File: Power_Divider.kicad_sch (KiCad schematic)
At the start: 46 parts, among them J16 Conn_01x02_Pin, J18 2118714-2, J9 2118714-2, P10 CONUFL001-SMD-T, P11 CONUFL001-SMD-T, P12 CONUFL001-SMD-T, P8 CONUFL001-SMD-T, P9 CONUFL001-SMD-T, U25 QPL9547, U7 MAX4995AAUT+T

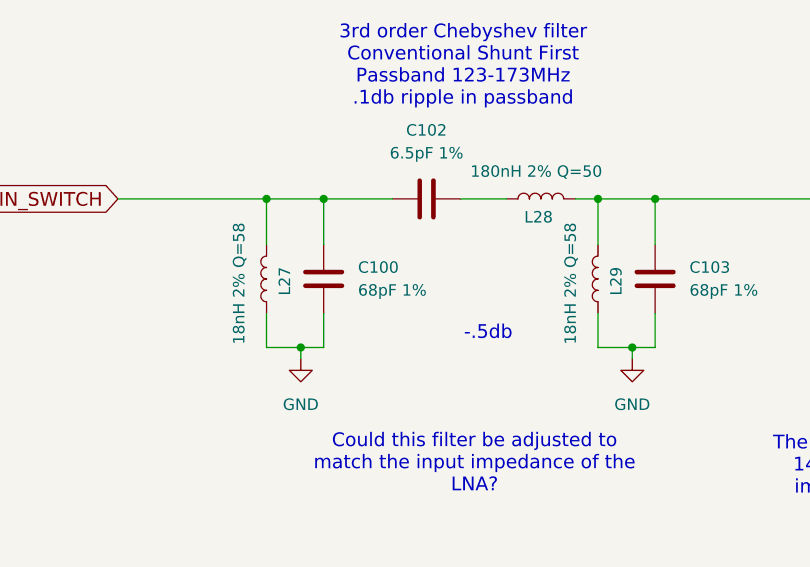
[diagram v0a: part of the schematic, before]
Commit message: Change the inductors on the RF input filter
Use lower resistance ones with higher Q.

Signed-off-by: Corey Minyard <corey@minyard.net>
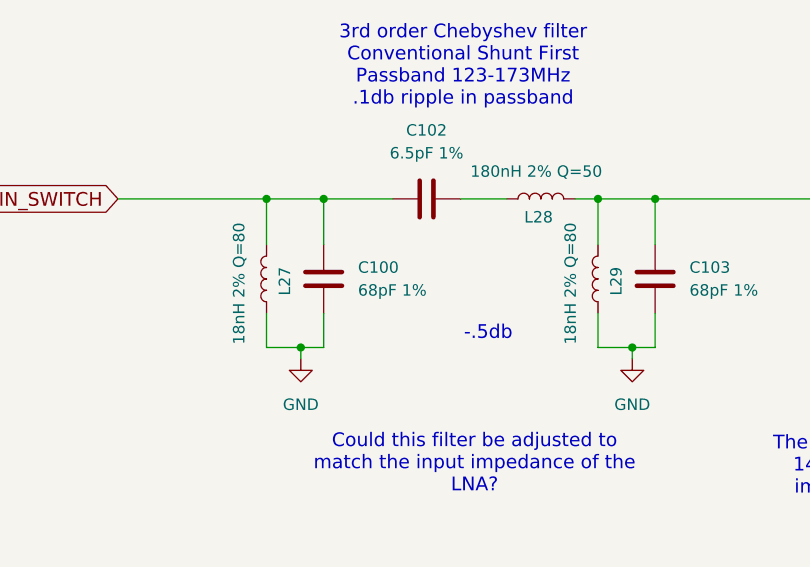
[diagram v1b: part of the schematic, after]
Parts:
- L27, L29: value 18nH 2% Q=58 -> 18nH 2% Q=80; footprint Inductor_SMD:L_0402_1005Metric_Pad0.77x0.64mm_HandSolder -> Inductor_SMD:L_0603_1608Metric_Pad1.05x0.95mm_HandSolder
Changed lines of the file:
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@@
 			)
 		)
-		(property "Value" "18nH 2% Q=58"
+		(property "Value" "18nH 2% Q=80"
 			(at 59.182 152.908 90)
 			(effects
@@
 			)
 		)
-		(property "Footprint" "Inductor_SMD:L_0402_1005Metric_Pad0.77x0.64mm_HandSolder"
+		(property "Footprint" "Inductor_SMD:L_0603_1608Metric_Pad1.05x0.95mm_HandSolder"
 			(at 62.23 152.4 0)
 			(effects
@@
 			)
 		)
-		(property "Value" "18nH 2% Q=58"
+		(property "Value" "18nH 2% Q=80"
 			(at 96.012 152.908 90)
 			(effects
@@
 			)
 		)
-		(property "Footprint" "Inductor_SMD:L_0402_1005Metric_Pad0.77x0.64mm_HandSolder"
+		(property "Footprint" "Inductor_SMD:L_0603_1608Metric_Pad1.05x0.95mm_HandSolder"
 			(at 99.06 152.4 0)
 			(effects

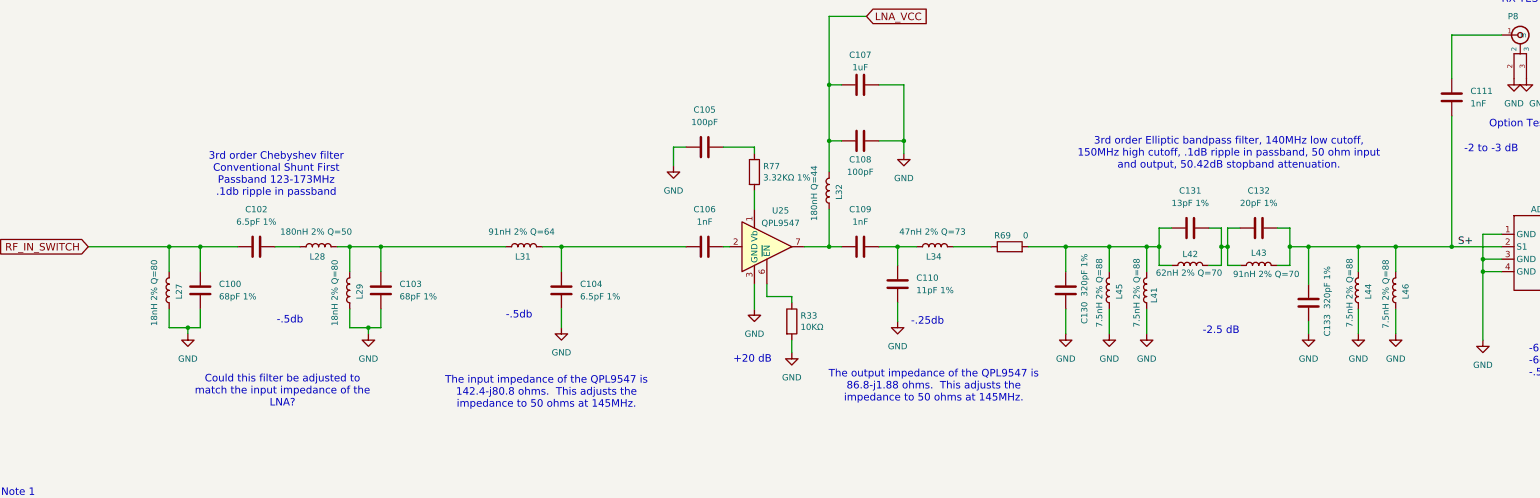
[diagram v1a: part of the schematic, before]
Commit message: Massive rework of filtering and inductors
Now that I know how inductors really work.

Signed-off-by: Corey Minyard <corey@minyard.net>
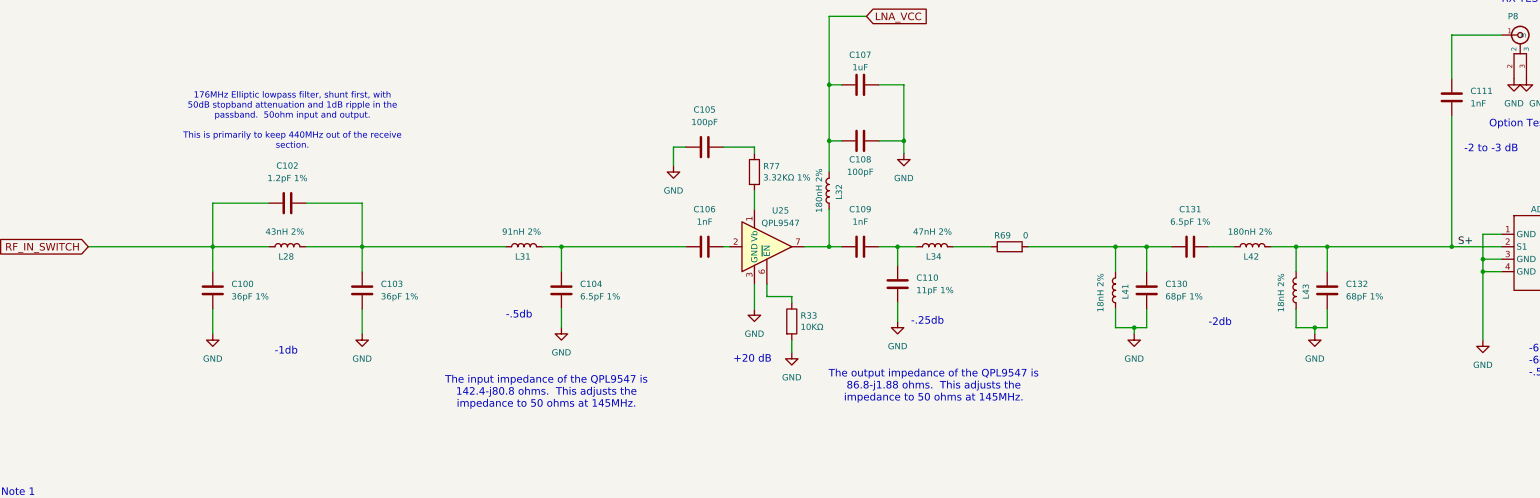
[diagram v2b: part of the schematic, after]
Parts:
- removed C133: 320pF 1%, Capacitor_SMD:C_0402_1005Metric_Pad0.74x0.62mm_HandSolder, symbol Device:C
- removed L27, L29: 18nH 2% Q=80, Inductor_SMD:L_0603_1608Metric_Pad1.05x0.95mm_HandSolder, symbol Device:L
- removed L44, L45, L46: 7.5nH 2% Q=88, Inductor_SMD:L_0603_1608Metric_Pad1.05x0.95mm_HandSolder, symbol Device:L
- C100, C103: value 68pF 1% -> 36pF 1%
- C102: value 6.5pF 1% -> 1.2pF 1%
- C130: value 320pF 1% -> 68pF 1%
- C131: value 13pF 1% -> 6.5pF 1%
- C132: value 20pF 1% -> 68pF 1%
- L28: value 180nH 2% Q=50 -> 43nH 2%
- L31: value 91nH 2% Q=64 -> 91nH 2%; footprint Inductor_SMD:L_0603_1608Metric_Pad1.05x0.95mm_HandSolder -> Inductor_SMD:L_0805_2012Metric_Pad1.05x1.20mm_HandSolder
- L32: value 180nH Q=44 -> 180nH 2%; footprint Inductor_SMD:L_0603_1608Metric_Pad1.05x0.95mm_HandSolder -> Inductor_SMD:L_0805_2012Metric_Pad1.05x1.20mm_HandSolder
- L34: value 47nH 2% Q=73 -> 47nH 2%
- L41: value 7.5nH 2% Q=88 -> 18nH 2%
- L42: value 62nH 2% Q=70 -> 180nH 2%; footprint Inductor_SMD:L_0805_2012Metric_Pad1.05x1.20mm_HandSolder -> Inductor_SMD:L_0805_2012Metric
- L43: value 91nH 2% Q=70 -> 18nH 2%; footprint Inductor_SMD:L_0805_2012Metric_Pad1.05x1.20mm_HandSolder -> Inductor_SMD:L_0603_1608Metric_Pad1.05x0.95mm_HandSolder
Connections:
- net GND: now also C132.1, L43.2
- net RF_IN_SWITCH: now also L28.2
- net S+: now also C132.2, L42.1; no longer C132.1
- net at C103.2, L28.1, L31.2: now also C102.1
- net at C130.2, C131.2, L41.1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: no longer L42.2
- new net: C131.1, L42.2
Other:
- note added: "-1db"
- note added: "-2db"
- note added: "176MHz Elliptic lowpass filter, shunt first, with 50dB stopband attenuation and 1dB ripple in the passband. 50ohm input and output. This is primarily to keep 440MHz out of the receive section."
- note removed: "-2.5 dB"
- note removed: "3rd order Chebyshev filter Conventional Shunt First Passband 123-173MHz .1db ripple in passband"
- note removed: "3rd order Elliptic bandpass filter, 140MHz low cutoff, 150MHz high cutoff, .1dB ripple in passband, 50 ohm input and output, 50.42dB stopband attenuation."
- note removed: "Could this filter be adjusted to match the input impedance of the LNA?"
- moved on the sheet: C100, C102, C103, L28

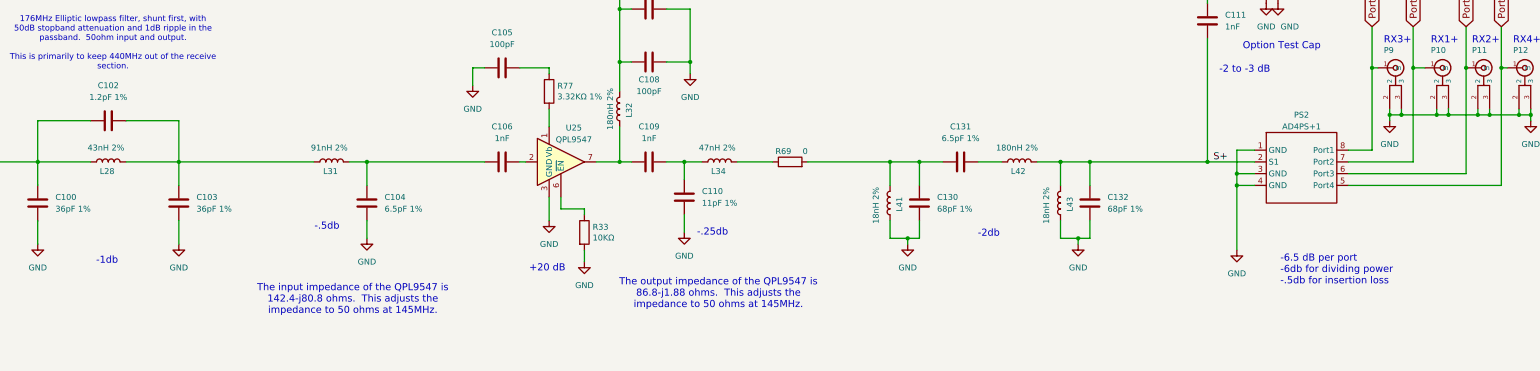
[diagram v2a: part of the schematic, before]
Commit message: Take into account capacitance of inductors
Signed-off-by: Corey Minyard <corey@minyard.net>
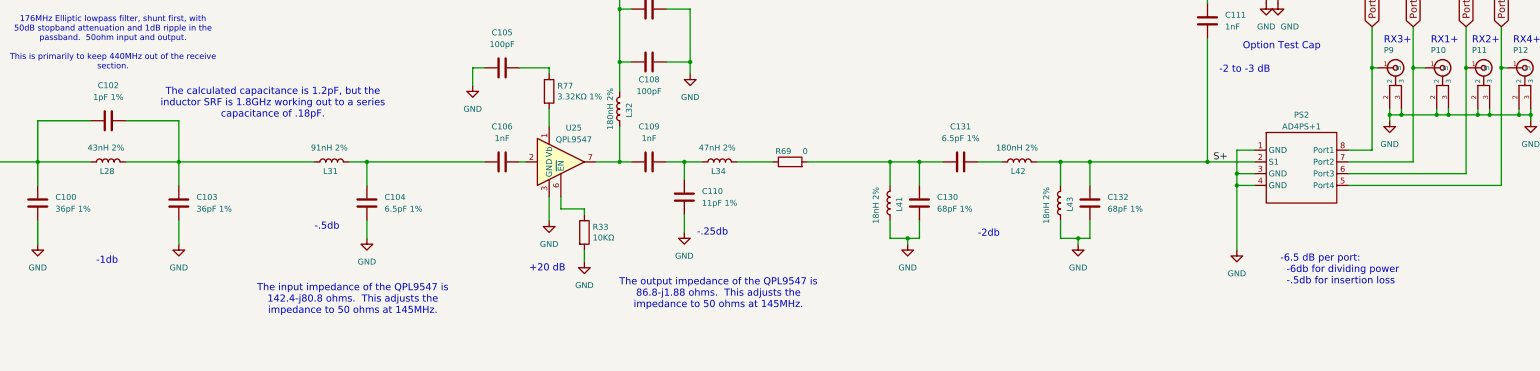
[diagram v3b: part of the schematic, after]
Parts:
- C102: value 1.2pF 1% -> 1pF 1%
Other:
- note added: "-6.5 dB per port: -6db for dividing power -.5db for insertion loss"
- note added: "The calculated capacitance is 1.2pF, but the inductor SRF is 1.8GHz working out to a series capacitance of .18pF."
- note removed: "-6.5 dB per port -6db for dividing power -.5db for insertion loss"
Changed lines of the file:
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@@
 		)
 	)
-	(text "-6.5 dB per port\n-6db for dividing power\n-.5db for insertion loss"
+	(text "-6.5 dB per port:\n  -6db for dividing power\n  -.5db for insertion loss"
 		(exclude_from_sim no)
 		(at 339.598 170.18 0)
@@
 		)
 	)
+	(text "The calculated capacitance is 1.2pF, but the\ninductor SRF is 1.8GHz working out to a series\ncapacitance of .18pF."
+		(exclude_from_sim no)
+		(at 121.92 130.81 0)
+		(effects
+			(font
+				(size 1.524 1.524)
+			)
+		)
+	)
 	(text "Note 3\nAll RF circuits must have at least 2 vias on \nall connections between PCB planes."
 		(exclude_from_sim no)
@@
 			)
 		)
-		(property "Value" "1.2pF 1%"
+		(property "Value" "1pF 1%"
 			(at 86.36 129.54 90)
 			(effects

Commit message: More simulation cleanups
Signed-off-by: Corey Minyard <corey@minyard.net>
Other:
- note added: "123-173MHz Chebychev bandpass filter, simulated from: * https://markimicrowave.com/technical-resources/tools/lc-filter-design-tool/ 3rd order, conventional shunt first, 123MHz low cutoff, 173MHz high cutoff, .10db ripple in passband, 50 ohm input, 50 ohm output impedance."
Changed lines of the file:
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@@
+		)
+	)
+	(text "123-173MHz Chebychev bandpass filter, simulated from:\n* https://markimicrowave.com/technical-resources/tools/lc-filter-design-tool/\n3rd order, conventional shunt first, 123MHz low cutoff, 173MHz high\ncutoff, .10db ripple in passband, 50 ohm input, 50 ohm output\nimpedance."
+		(exclude_from_sim no)
+		(at 273.812 127.254 0)
+		(effects
+			(font
+				(size 1.27 1.27)
+			)
 		)
 	)

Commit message: Minor fixes for BOM values
Signed-off-by: Corey Minyard <corey@minyard.net>
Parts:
- R69: value 0 -> 0Ω
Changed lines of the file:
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@@
 			)
 		)
-		(property "Value" "0"
+		(property "Value" "0Ω"
 			(at 237.49 141.224 90)
 			(effects

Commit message: A bunch of work on component selections
And little fixups for things I found.

Signed-off-by: Corey Minyard <corey@minyard.net>
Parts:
- C102: value 1pF 1% -> 1pF ±.05
- C104, C131: value 6.5pF 1% -> 6.5pF ±.1
- R33, R77: footprint Resistor_SMD:R_0603_1608Metric_Pad0.98x0.95mm_HandSolder -> Resistor_SMD:R_0402_1005Metric_Pad0.72x0.64mm_HandSolder
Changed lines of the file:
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@@
 			)
 		)
-		(property "Footprint" "Resistor_SMD:R_0603_1608Metric_Pad0.98x0.95mm_HandSolder"
+		(property "Footprint" "Resistor_SMD:R_0402_1005Metric_Pad0.72x0.64mm_HandSolder"
 			(at 179.832 128.27 90)
 			(effects
@@
 			)
 		)
-		(property "Footprint" "Resistor_SMD:R_0603_1608Metric_Pad0.98x0.95mm_HandSolder"
+		(property "Footprint" "Resistor_SMD:R_0402_1005Metric_Pad0.72x0.64mm_HandSolder"
 			(at 187.452 158.75 90)
 			(effects
@@
 			)
 		)
-		(property "Value" "6.5pF 1%"
+		(property "Value" "6.5pF ±.1"
 			(at 146.05 153.6699 0)
 			(effects
@@
 			)
 		)
-		(property "Value" "6.5pF 1%"
+		(property "Value" "6.5pF ±.1"
 			(at 270.51 138.43 90)
 			(effects
@@
 			)
 		)
-		(property "Value" "1pF 1%"
+		(property "Value" "1pF ±.05"
 			(at 86.36 129.54 90)
 			(effects

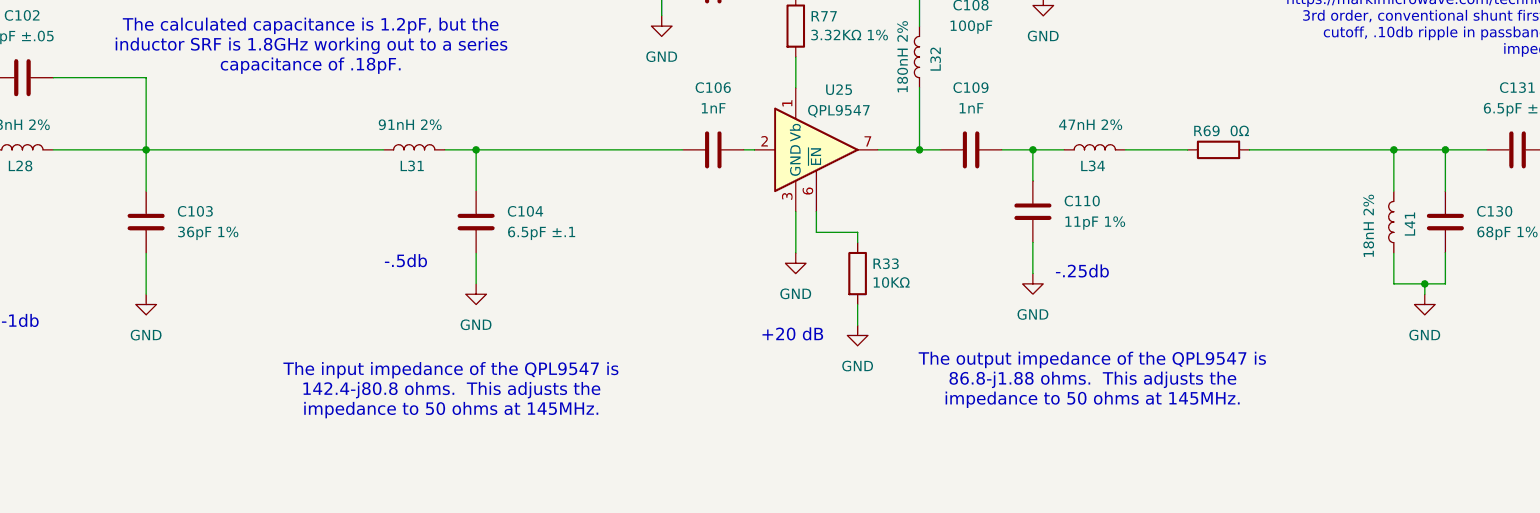
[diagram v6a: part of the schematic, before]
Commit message: Add some more UF.L connectors, clean up more stuff
Allow access to some more points in the RF chain.

Signed-off-by: Corey Minyard <corey@minyard.net>
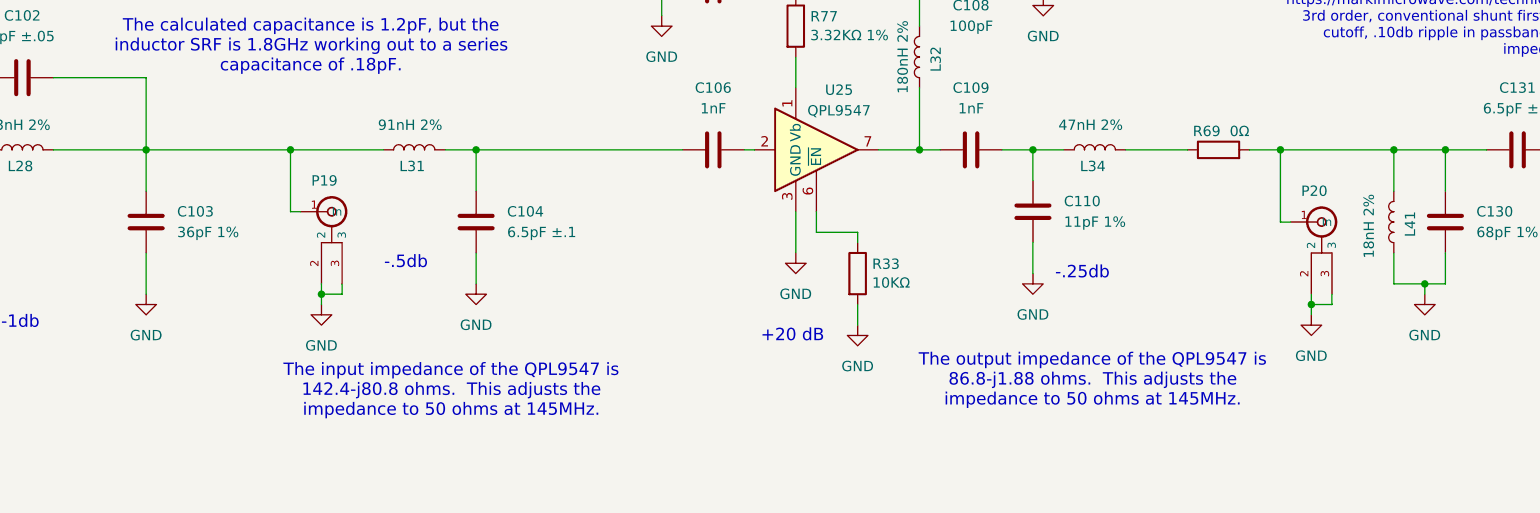
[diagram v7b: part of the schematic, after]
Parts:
- added P19, P20: CONUFL001-SMD-T, PacSatDev_misc:CONN1_CONUFL_TEC, symbol PACSAT_DEV_misc:U_FL
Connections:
- net GND: now also P19.2, P19.3, P20.2, P20.3
- net at C102.1, C103.2, L28.1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: now also P19.1 (In)
- net at C130.2, C131.2, L41.1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: now also P20.1 (In)

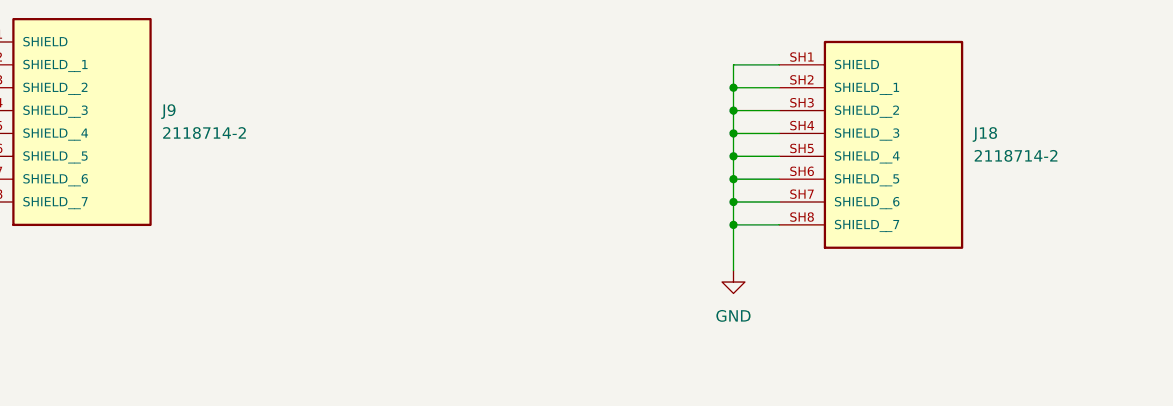
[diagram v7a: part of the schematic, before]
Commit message: Renumber shields and PC104 sockets
Separate out shields into their own designator category.

Make the PC104 sockets J1 and J2 to make it easier to move to other
boards.

Signed-off-by: Corey Minyard <corey@minyard.net>
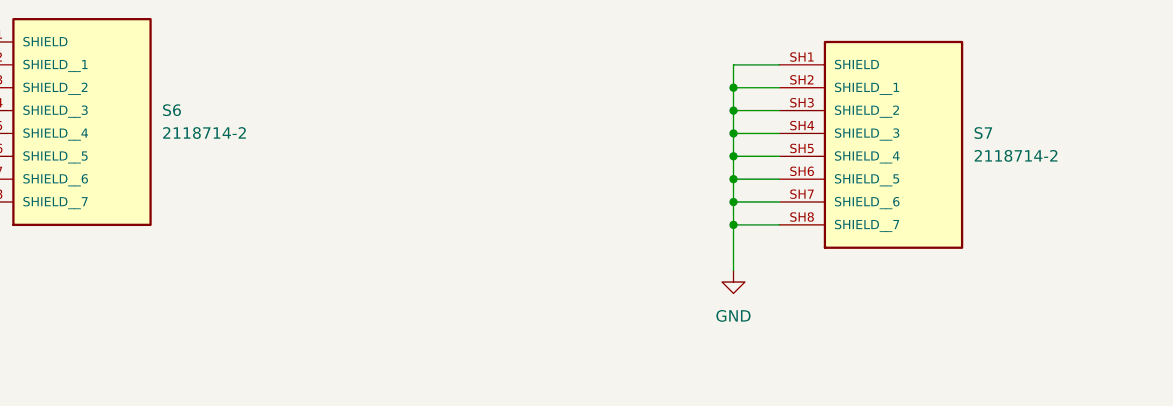
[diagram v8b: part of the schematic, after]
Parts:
- renumbered J9 to S6, J18 to S7
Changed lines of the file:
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@@
 		(dnp no)
 		(fields_autoplaced yes)
-		(property "Reference" "J9"
+		(property "Reference" "S6"
 			(at 199.39 44.4499 0)
 			(effects
@@
 			(project "PacSat_AFSK"
 				(path "/cc9f42d2-6985-41ac-acab-5ab7b01c5b38/9af0eacb-5211-4e23-85d7-9c1805bbe6a4"
-					(reference "J9")
+					(reference "S6")
 					(unit 1)
 				)
@@
 		(dnp no)
 		(fields_autoplaced yes)
-		(property "Reference" "J18"
+		(property "Reference" "S7"
 			(at 289.56 46.9899 0)
 			(effects
@@
 			(project "PacSat_AFSK"
 				(path "/cc9f42d2-6985-41ac-acab-5ab7b01c5b38/9af0eacb-5211-4e23-85d7-9c1805bbe6a4"
-					(reference "J18")
-					(unit 1)
-				)
+					(reference "S7")
+					(unit 1)
+				)
